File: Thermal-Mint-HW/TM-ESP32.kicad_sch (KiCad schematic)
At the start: 2 parts, among them U3 ESP32-C3

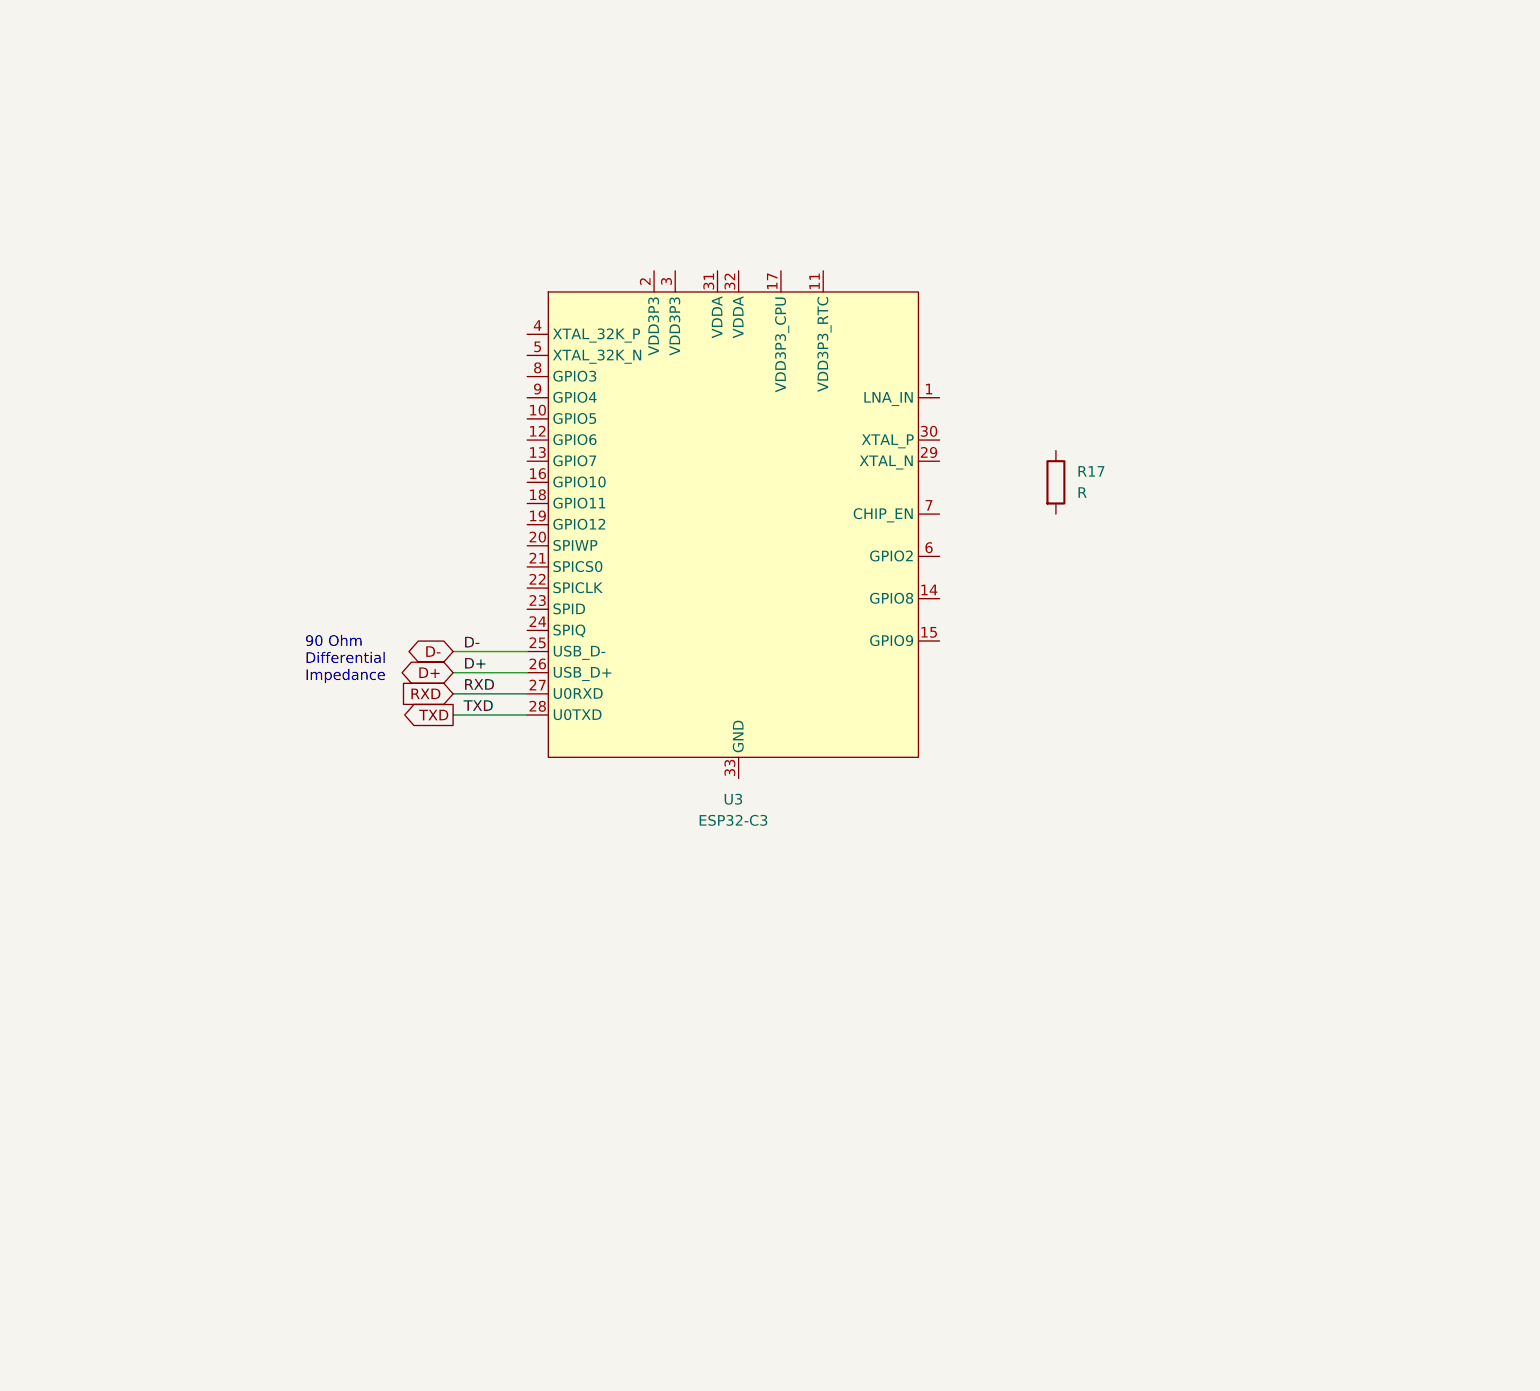
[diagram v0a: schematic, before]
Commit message: WIP commit, Adding connectors and memory
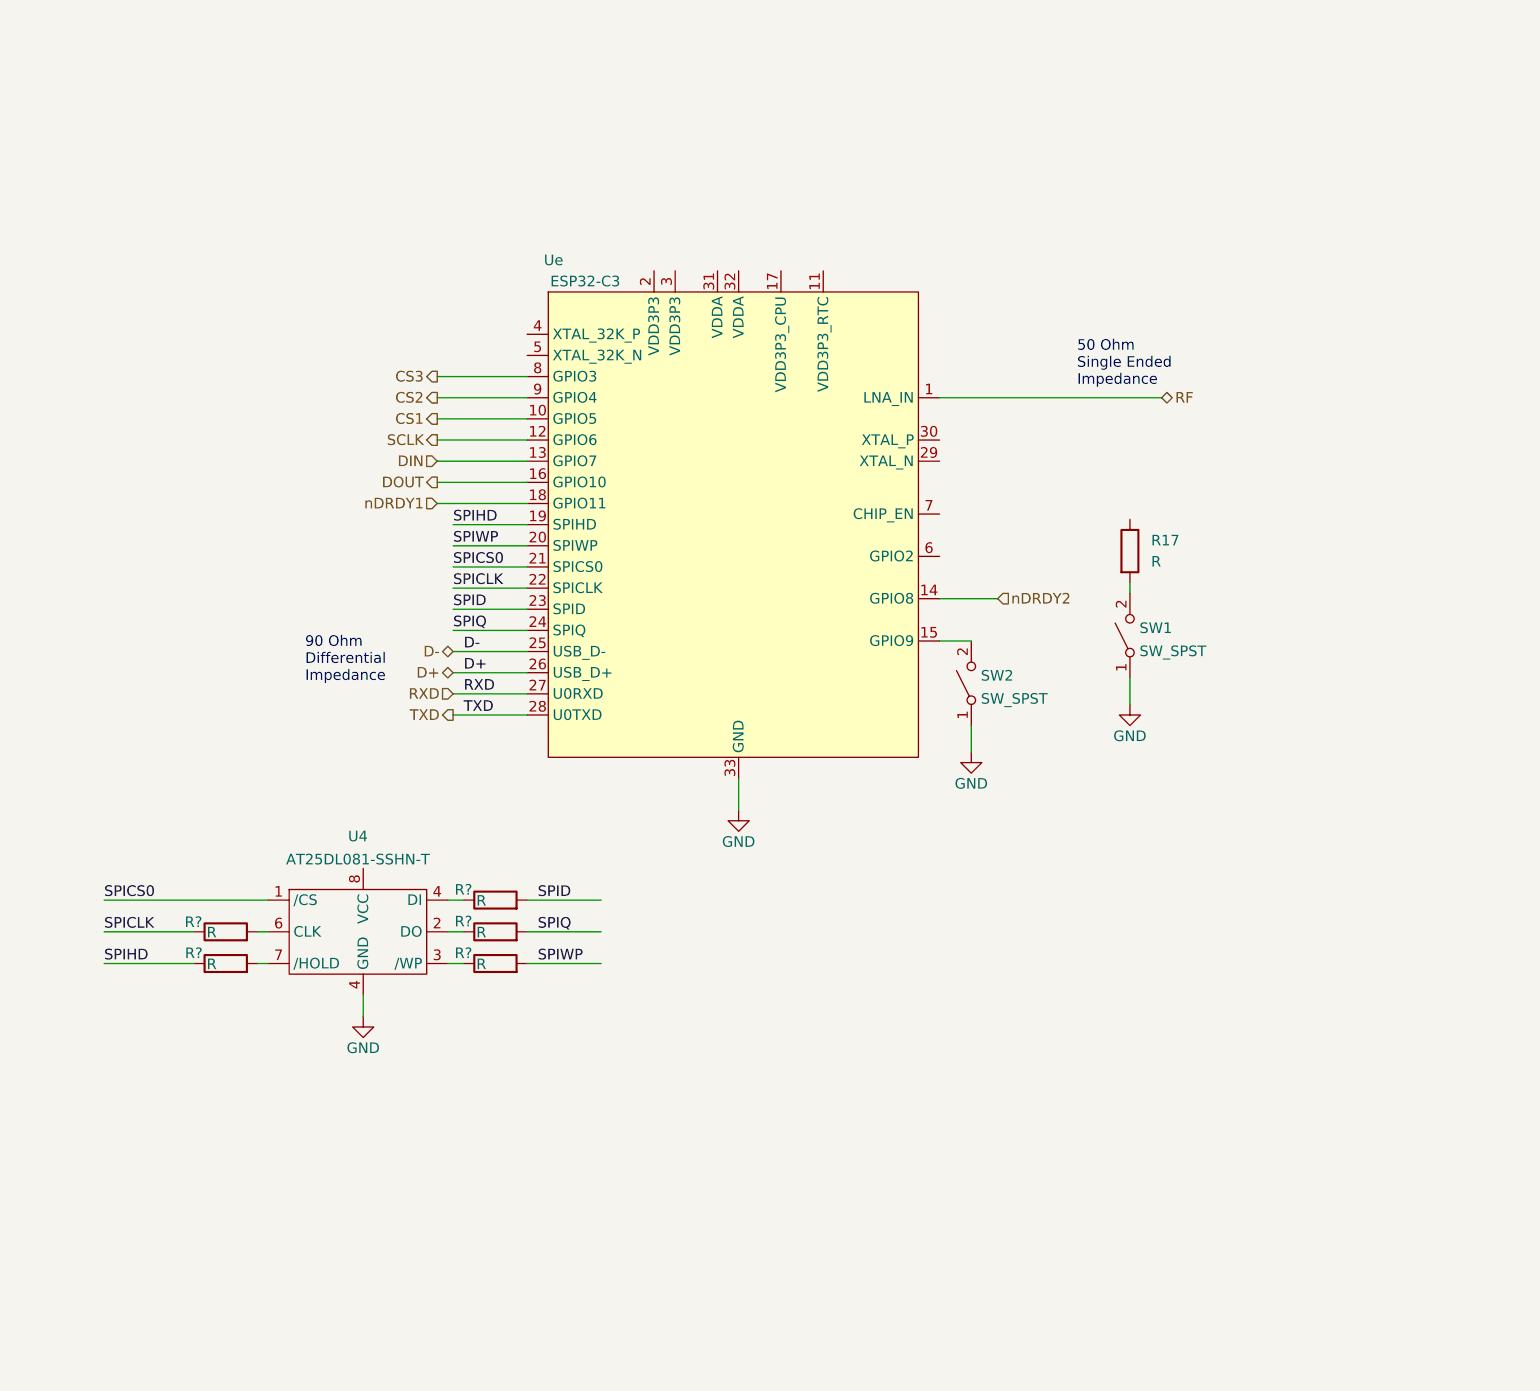
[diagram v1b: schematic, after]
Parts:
- added R? (x5): R, Resistor_SMD:R_0603_1608Metric_Pad1.05x0.95mm_HandSolder, symbol Device:R
- added SW1, SW2: SW_SPST, ThermalMint:SW_SPST_PTS647, symbol Switch:SW_SPST
- added U4: AT25DL081-SSHN-T, Package_SO:SOIC-8_3.9x4.9mm_P1.27mm, symbol ThermalMint:AT25DL081-SSHN-T
- R17: footprint (none) -> Resistor_SMD:R_0603_1608Metric_Pad1.05x0.95mm_HandSolder
- renumbered U3 to Ue
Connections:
- net at R17.2: now also SW1.2 (B)
- net RF: now reaches Ue.1 (LNA_IN)
- net CS1: now reaches Ue.10 (GPIO5)
- net SCLK: now reaches Ue.12 (GPIO6)
- net DIN: now reaches Ue.13 (GPIO7)
- net nDRDY2: now reaches Ue.14 (GPIO8)
- net at Ue.15 (GPIO9): now also SW2.2 (B)
- net DOUT: now reaches Ue.16 (GPIO10)
- net nDRDY1: now reaches Ue.18 (GPIO11)
- net SPIHD: now reaches Ue.19 (GPIO12)
- net SPIHD: now also R?.1
- net SPIWP: now reaches Ue.20 (GPIO13)
- net SPIWP: now also R?.2
- net SPICS0: now reaches Ue.21 (GPIO14)
- net SPICS0: now also U4.1 (/CS)
- net SPICLK: now reaches Ue.22 (GPIO15)
- net SPICLK: now also R?.1
- net SPID: now reaches Ue.23 (GPIO16)
- net SPID: now also R?.2
- net SPIQ: now reaches Ue.24 (GPIO17)
- net SPIQ: now also R?.2
- net GND: now reaches Ue.33 (GND)
- net GND: now also SW1.1 (A), SW2.1 (A), U4.4 (GND)
- net CS3: now reaches Ue.8 (GPIO3)
- net CS2: now reaches Ue.9 (GPIO4)
- new net: R?.1, U4.2 (DO)
- new net: R?.1, U4.3 (/WP)
- new net: R?.1, U4.4 (GND)
- new net: R?.2, U4.6 (CLK)
- new net: R?.2, U4.7 (/HOLD)
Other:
- note added: "50 Ohm Single Ended Impedance"
- moved on the sheet: R17

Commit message: Clean up of output circuits
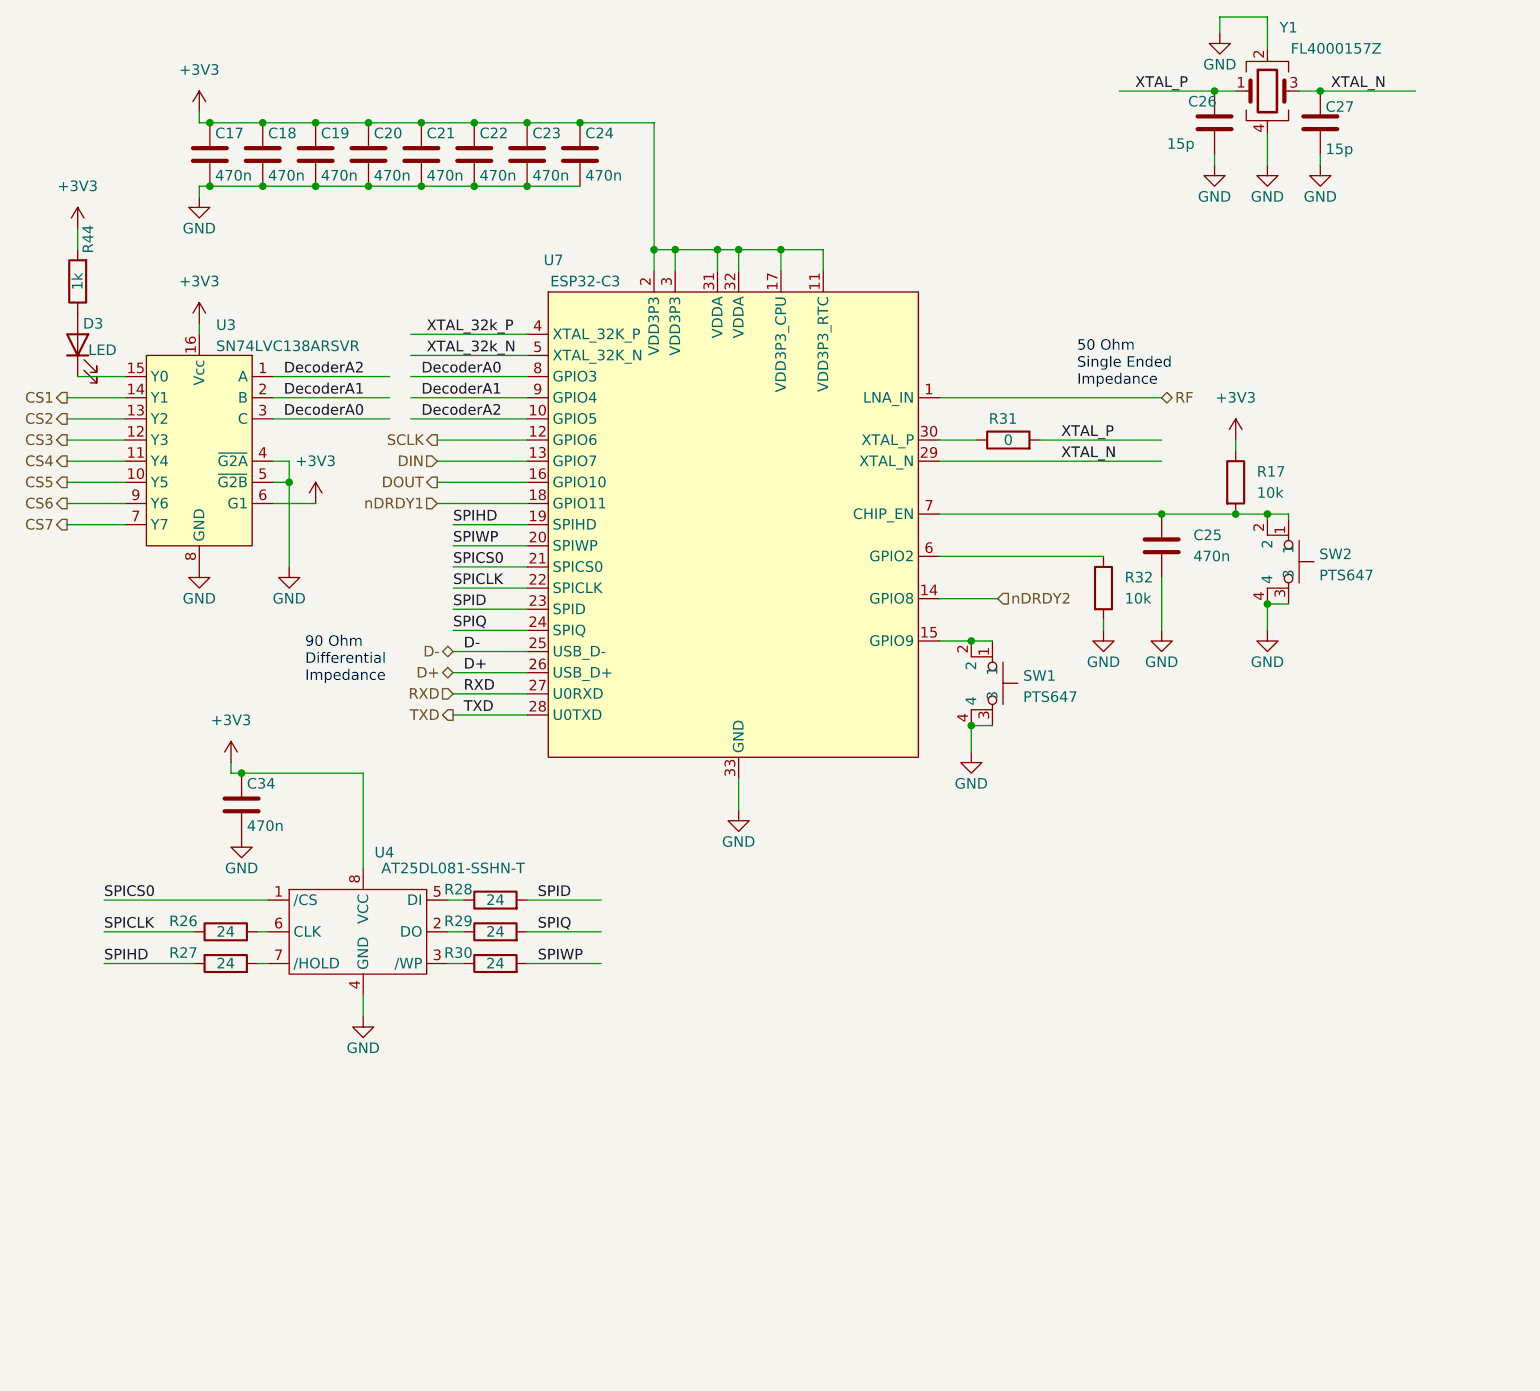
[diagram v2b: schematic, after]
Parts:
- removed SW1, SW2: SW_SPST, ThermalMint:SW_SPST_PTS647, symbol Switch:SW_SPST
- added C17, C18, C19, C20, C21, C22, C23, C24, C25, C34: 470n, Capacitor_SMD:C_0603_1608Metric_Pad1.08x0.95mm_HandSolder, symbol Device:C
- added C26, C27: 15p, Capacitor_SMD:C_0603_1608Metric_Pad1.08x0.95mm_HandSolder, symbol Device:C
- added D3: LED, LED_SMD:LED_0603_1608Metric, symbol Device:LED
- added R31: 0, Resistor_SMD:R_0603_1608Metric_Pad0.98x0.95mm_HandSolder, symbol Device:R
- added R32: 10k, Resistor_SMD:R_0603_1608Metric_Pad0.98x0.95mm_HandSolder, symbol Device:R
- added R44: 1k, Resistor_SMD:R_0603_1608Metric_Pad0.98x0.95mm_HandSolder, symbol Device:R
- added SW1, SW2: PTS647, ThermalMint:SW_SPST_PTS647, symbol ThermalMint:PTS647
- added U3: SN74LVC138ARSVR, ThermalMint:UQFN16 - RSV0016A, symbol ThermalMint:SN74LVC138ARSVR
- added Y1: FL4000157Z, Crystal:Crystal_SMD_3225-4Pin_3.2x2.5mm, symbol Device:Crystal_GND24
- R17: value R -> 10k; footprint Resistor_SMD:R_0603_1608Metric_Pad1.05x0.95mm_HandSolder -> Resistor_SMD:R_0603_1608Metric_Pad0.98x0.95mm_HandSolder
- R26, R27, R28, R29, R30: renamed from R?; value R -> 24; footprint Resistor_SMD:R_0603_1608Metric_Pad1.05x0.95mm_HandSolder -> Resistor_SMD:R_0603_1608Metric_Pad0.98x0.95mm_HandSolder
- renumbered Ue to U7
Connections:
- net CS1: now also U3.14 (Y1); no longer U7.10 (GPIO5)
- net CS2: now also U3.13 (Y2); no longer U7.9 (GPIO4)
- net CS3: now also U3.12 (Y3); no longer U7.8 (GPIO3)
- net GND: now also C17.2, C18.2, C19.2, C20.2, C21.2, C22.2, C23.2, C24.2, C25.2, C26.2, C27.2, C34.2, R32.2, SW1.3, SW1.4, SW2.3, SW2.4, U3.4 (~{G2A}), U3.5 (~{G2B}), U3.8 (GND), Y1.2, Y1.4
- net +3V3: now reaches R17.1
- net +3V3: now also U4.8 (VCC), U7.11 (VDD3P3_RTC), U7.17 (VDD3P3_CPU), U7.2 (VDD3P3), U7.3 (VDD3P3), U7.31 (VDDA), U7.32 (VDDA), C17.1, C18.1, C19.1, C20.1, C21.1, C22.1, C23.1, C24.1, C34.1, R44.2, U3.16 (Vcc), U3.6 (G1)
- net at R17.2: now also U7.7 (CHIP_EN), C25.1, SW2.1, SW2.2
- net at U7.15 (GPIO9): now also SW1.1, SW1.2
- net XTAL_N: now reaches U7.29 (XTAL_N)
- net XTAL_N: now also C27.1, Y1.3
- net at U7.30 (XTAL_P): now also R31.1
- net XTAL_32k_P: now reaches U7.4 (GPIO0)
- net XTAL_32k_N: now reaches U7.5 (GPIO1)
- net at U7.6 (GPIO2): now also R32.1
- net at R28.1: now also U4.5 (DI); no longer U4.4 (GND)
- new net: D3.2 (A), R44.1
- new net: D3.1 (K), U3.15 (Y0)
- new net CS4: U3.11 (Y4)
- new net CS5: U3.10 (Y5)
- new net CS6: U3.9 (Y6)
- new net CS7: U3.7 (Y7)
- new net DecoderA0: U3.3 (C), U7.8 (GPIO3)
- new net DecoderA1: U3.2 (B), U7.9 (GPIO4)
- new net DecoderA2: U3.1 (A), U7.10 (GPIO5)
- new net XTAL_P: C26.1, R31.2, Y1.1
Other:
- moved on the sheet: R17

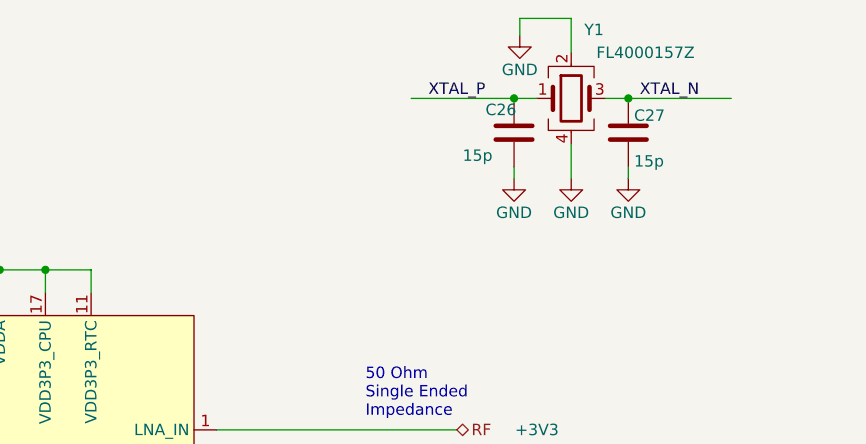
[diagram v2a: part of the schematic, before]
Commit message: Cleanup of Rev1 schematics for review
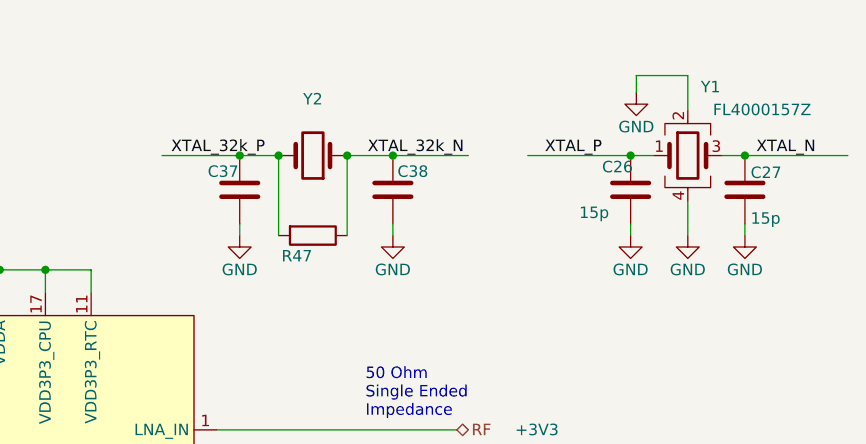
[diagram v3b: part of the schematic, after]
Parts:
- added C37, C38: (no value), Capacitor_SMD:C_0603_1608Metric_Pad1.08x0.95mm_HandSolder, symbol Device:C
- added R47: (no value), Resistor_SMD:R_0603_1608Metric_Pad0.98x0.95mm_HandSolder, symbol Device:R
- added Y2: (no value), symbol Device:Crystal
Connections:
- net GND: now also C37.2, C38.2
- net XTAL_32k_N: now also C38.1, R47.1, Y2.1
- net XTAL_32k_P: now also C37.1, R47.2, Y2.2
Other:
- moved on the sheet: C26, C27, Y1
